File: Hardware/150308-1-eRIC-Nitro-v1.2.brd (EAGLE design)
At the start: 55.2 x 25.4 mm, 39 parts, among them IC1 ATmega328P-AU, IC2 MIC5205-3.3, K1 M12PTH, K2 M12PTH, K4 FTDI Basic, K6 SMA_EDGE, X1 8MHz

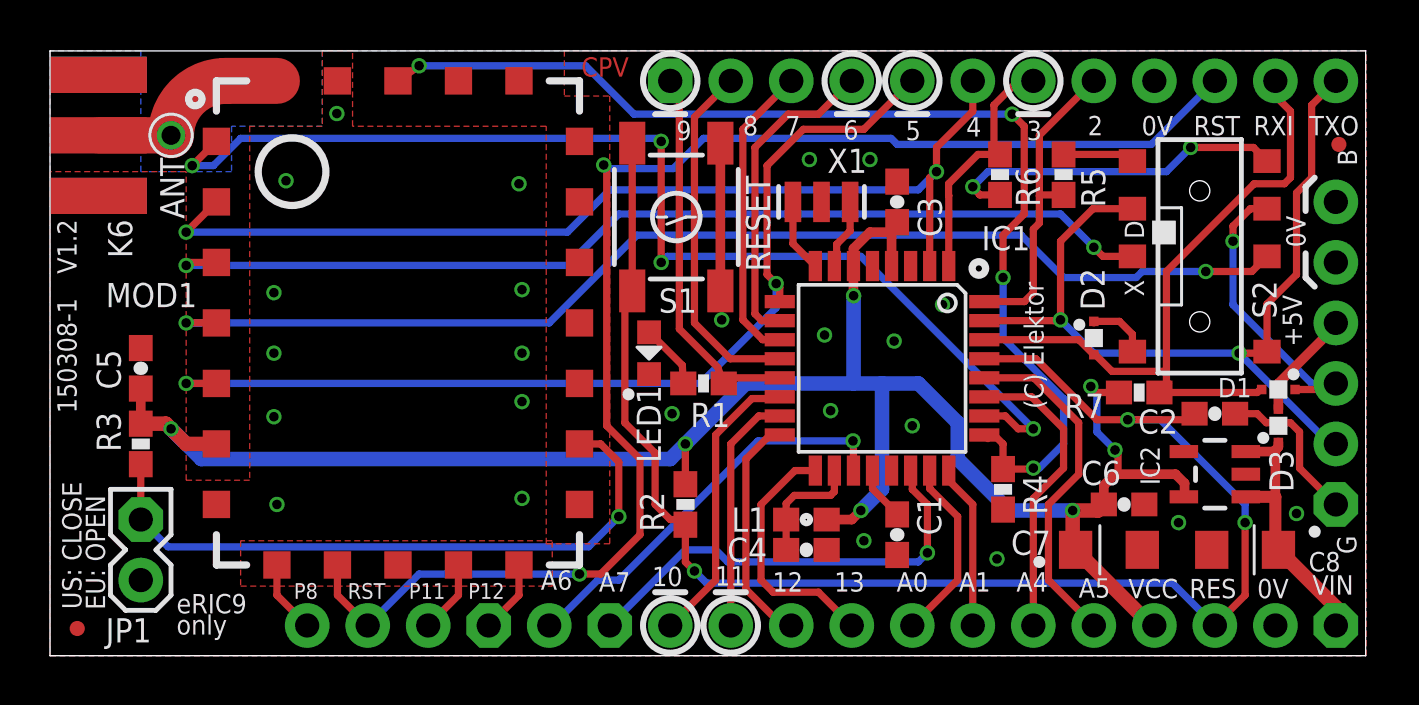
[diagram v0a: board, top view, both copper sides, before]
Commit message: Small cosmetic changes, new bootloader
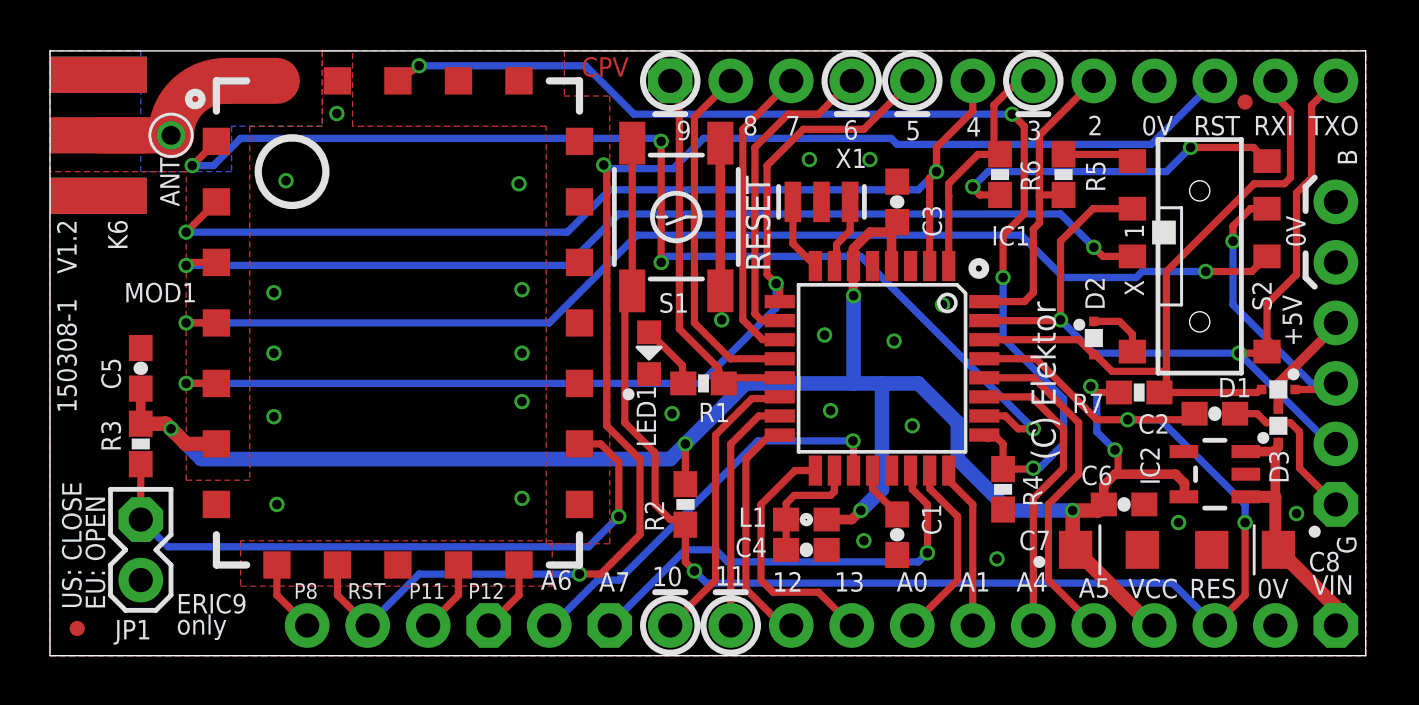
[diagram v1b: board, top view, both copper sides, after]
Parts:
- IC2: device SparkFun:SOT23-5 -> 150308-1-eRIC-Nitro:SOT23-5
- moved FID1 4.32 mm to (25.4, 23.2)
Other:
- board text added: "1"
- board text added: "ERIC4: 433 MHz ERIC9: 868/915 MHz (JP1)"
- board text added: "ERIC9"
- board text removed: "D"
- board text removed: "PCB design by"
- board text removed: "eRIC4: 433 MHz eRIC9: 868/915 MHz (JP1)"
- board text removed: "eRIC9"
- board text removed: "open hardware"
